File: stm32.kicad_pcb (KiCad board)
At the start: 2 copper layers, 16 parts, among them J1 TC2030, SW1 SW_Push, U1 STM32F411CEUx, Y1 Crystal_GND24

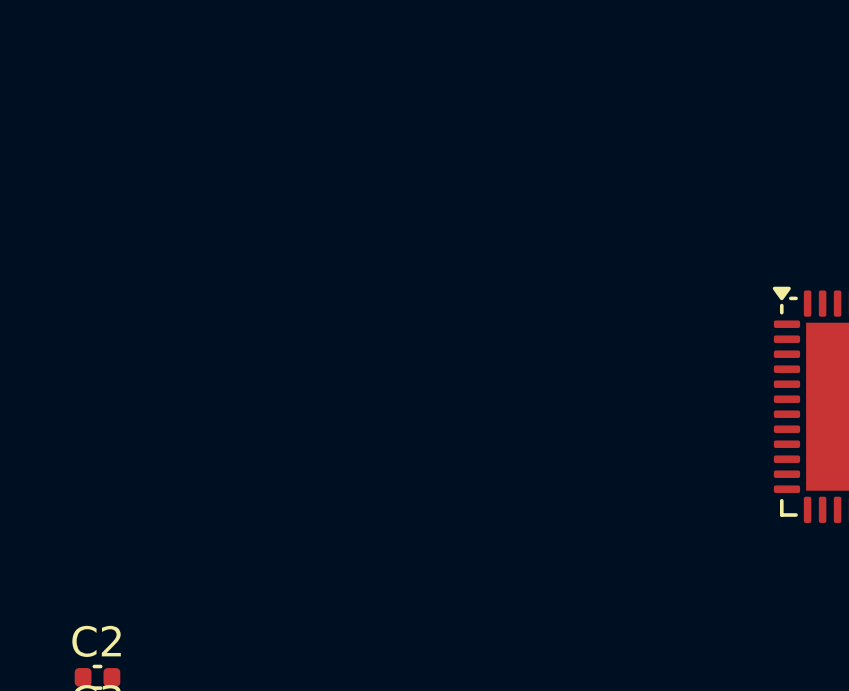
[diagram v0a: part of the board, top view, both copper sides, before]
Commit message: SPI section: place BMI088, BMP388, W25Q128 symbols + decoupling + HOLD/WP pull-ups
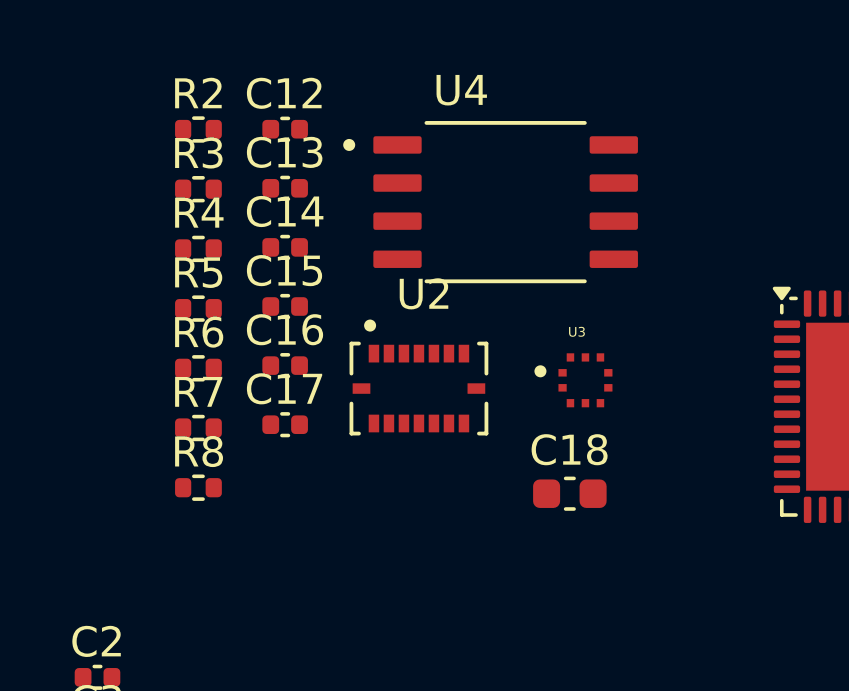
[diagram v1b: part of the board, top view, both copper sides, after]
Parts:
- added C12: 1u, Capacitor_SMD:C_0402_1005Metric, F.Cu at (131.7, 45.9)
- added C13: 100n, Capacitor_SMD:C_0402_1005Metric, F.Cu at (131.7, 47.8)
- added C14: 100n, Capacitor_SMD:C_0402_1005Metric, F.Cu at (131.7, 49.8)
- added C15: 100n, Capacitor_SMD:C_0402_1005Metric, F.Cu at (131.7, 51.8)
- added C16: 100n, Capacitor_SMD:C_0402_1005Metric, F.Cu at (131.7, 53.7)
- added C17: 100n, Capacitor_SMD:C_0402_1005Metric, F.Cu at (131.7, 55.7)
- added C18: 4.7u, Capacitor_SMD:C_0603_1608Metric, F.Cu at (141.2, 58.0)
- added R2: 10k, Resistor_SMD:R_0402_1005Metric, F.Cu at (128.8, 45.9)
- added R3: 10k, Resistor_SMD:R_0402_1005Metric, F.Cu at (128.8, 47.9)
- added R4: 10k, Resistor_SMD:R_0402_1005Metric, F.Cu at (128.8, 49.8)
- added R5: 10k, Resistor_SMD:R_0402_1005Metric, F.Cu at (128.8, 51.8)
- added R6: 10k, Resistor_SMD:R_0402_1005Metric, F.Cu at (128.8, 53.8)
- added R7: 10k, Resistor_SMD:R_0402_1005Metric, F.Cu at (128.8, 55.8)
- added R8: 10k, Resistor_SMD:R_0402_1005Metric, F.Cu at (128.8, 57.8)
- added U2: BMI088, Custom_Library:BMI088, F.Cu at (136.2, 54.5)
- added U3: BMP388, Custom_Library:BMP388, F.Cu at (141.7, 54.2)
- added U4: W25Q128JVSIQ, Custom_Library:W25Q128, F.Cu at (139.1, 48.3)
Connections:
- U1 pad 11: unconnected-(U1-PA1-Pad11) -> /FLASH
- U1 pad 12: unconnected-(U1-PA2-Pad12) -> /BMP
- U1 pad 13: unconnected-(U1-PA3-Pad13) -> /GYRO
- U1 pad 14: unconnected-(U1-PA4-Pad14) -> /ACCEL
- U1 pad 15: unconnected-(U1-PA5-Pad15) -> /SPI1_SCK
- U1 pad 16: unconnected-(U1-PA6-Pad16) -> /SPI1_MISO
- U1 pad 17: unconnected-(U1-PA7-Pad17) -> /SPI1_MOSI
- U1 pad 18: unconnected-(U1-PB0-Pad18) -> /ACCEL_INT
- U1 pad 19: unconnected-(U1-PB1-Pad19) -> /GYRO_INT

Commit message: small update
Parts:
- added J2: USB_C_Receptacle_PowerOnly_6P, Connector_USB:USB_C_Receptacle_GCT_USB4125-xx-x_6P_TopMnt_Horizontal, F.Cu at (121.0, 35.0)
- added R10: 10k, Resistor_SMD:R_0402_1005Metric, F.Cu at (107.8, 34.4)
- added R11: 1k, Resistor_SMD:R_0402_1005Metric, F.Cu at (107.8, 36.4)
- added R12: 1k, Resistor_SMD:R_0402_1005Metric, F.Cu at (107.8, 38.4)
- added R23: 5.1k, Resistor_SMD:R_0402_1005Metric, F.Cu at (107.8, 40.4)
- added R24: 5.1k, Resistor_SMD:R_0402_1005Metric, F.Cu at (107.8, 42.4)
- added R9: 4.7k, Resistor_SMD:R_0402_1005Metric, F.Cu at (107.8, 32.4)
- added U5: TP4056-42-ESOP8, Package_SO:SOIC-8-1EP_3.9x4.9mm_P1.27mm_EP2.41x3.3mm_ThermalVias, F.Cu at (117.8, 48.7)
- added U6: AP63203WU, Package_TO_SOT_SMD:TSOT-23-6, F.Cu at (105.4, 47.8)

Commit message: fleshed out buck
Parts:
- added C19: 1u, Capacitor_SMD:C_0402_1005Metric, F.Cu at (120.6, 94.3)
- added C20: 10u, Capacitor_SMD:C_0603_1608Metric, F.Cu at (129.0, 83.6)
- added C21: 22u, Capacitor_SMD:C_0603_1608Metric, F.Cu at (129.0, 86.1)
- added D1: RED_LED, LED_SMD:LED_Kingbright_KPBD-3224, F.Cu at (121.1, 85.5)
- added D2: GREEN_LED, LED_SMD:LED_Kingbright_KPBD-3224, F.Cu at (125.1, 85.5)
- added IC1: LTC3621EMS8E-3.3#PBF, Custom_Library:LTC3621EMS8E-3.3#PBF, F.Cu at (122.8, 91.0)
- added L1: 4.7u, Inductor_SMD:L_Coilcraft_XxL4020, F.Cu at (129.3, 91.5)

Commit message: next steps
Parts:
- added D3: SS14, Diode_SMD:D_SMA, F.Cu at (147.5, 92.5)
- added D4: 1N4148WS, Diode_SMD:D_SOD-323, F.Cu at (147.5, 88.5)
- added Q1: DMG2305UX, Custom_Library:DMG2305UX, F.Cu at (142.0, 89.5)
- added R13: 100k, Resistor_SMD:R_0402_1005Metric, F.Cu at (147.0, 84.0)
- Y1: value Crystal_GND24 -> 25MHz
- moved J2 76.5 mm to (137.7, 109.7)
- moved SW1 31.6 mm to (120.5, 73.0), turned to 180 degrees
- moved C8 27.5 mm to (138.2, 85.0)
- moved U1 24.2 mm to (136.8, 73.9)
- moved C2 20.4 mm to (139.5, 79.0), turned to -90 degrees
- moved C20 17.3 mm to (142.0, 95.0), turned to -90 degrees
- moved C3 17.2 mm to (142.0, 71.0)
- moved IC1 15.4 mm to (137.8, 94.5), turned to 180 degrees
- moved C10 14.9 mm to (149.9, 64.2)
- moved C11 14.9 mm to (149.9, 66.2)
- moved Y1 14.9 mm to (154.0, 63.5)
- moved C19 12.5 mm to (133.0, 95.0), turned to 180 degrees
- moved L1 12.2 mm to (139.0, 99.0)
- moved C6 10.8 mm to (128.0, 75.5), turned to -90 degrees
- moved J1 8.68 mm to (155.3, 92.1)
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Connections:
- net +5V renamed /VBUS_5V
- C19 pad 1: GND -> Net-(IC1-INTVCC)
- C19 pad 2: Net-(IC1-INTVCC) -> GND
- IC1 pad 7: unconnected-(IC1-MODE/SYNC-Pad7) -> Net-(IC1-INTVCC)
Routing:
- net +3.3V: track 0.00 -> 39.6 mm
- net /NRST: track 0.00 -> 18.3 mm
- net /VIN_BUCK: track 0.00 -> 10.5 mm
- net GND: track 0.00 -> 8.89 mm
- net /GATE_LS: track 0.00 -> 8.05 mm
- net Net-(IC1-SW): track 0.00 -> 3.58 mm
- net Net-(IC1-INTVCC): track 0.00 -> 2.91 mm

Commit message: Assign J5 UART header footprint; import netlist to PCB for layout
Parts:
- added C22: 0.1u, Capacitor_SMD:C_0402_1005Metric, F.Cu at (133.5, 23.9)
- added C23: 100n, Capacitor_SMD:C_0402_1005Metric, F.Cu at (133.5, 25.9)
- added C24: 100n, Capacitor_SMD:C_0402_1005Metric, F.Cu at (133.5, 27.8)
- added D5: LED, LED_SMD:LED_0603_1608Metric, F.Cu at (123.9, 40.6)
- added J3: Conn_01x02, Connector_JST:JST_PH_S2B-PH-SM4-TB_1x02-1MP_P2.00mm_Horizontal, F.Cu at (127.0, 28.5)
- added J4: Conn_01x02, Connector_PinHeader_2.54mm:PinHeader_1x02_P2.54mm_Vertical, F.Cu at (135.0, 36.5)
- added J5: Conn_01x03, Connector_PinHeader_2.54mm:PinHeader_1x03_P2.54mm_Vertical, F.Cu at (114.5, 31.7)
- added R14: 100, Resistor_SMD:R_0402_1005Metric, F.Cu at (120.4, 23.9)
- added R15: 1k, Resistor_SMD:R_0402_1005Metric, F.Cu at (120.4, 25.9)
- added R16: 1k, Resistor_SMD:R_0402_1005Metric, F.Cu at (120.4, 27.9)
- added R17: 10k, Resistor_SMD:R_0402_1005Metric, F.Cu at (120.4, 29.9)
- added R18: 100k, Resistor_SMD:R_0402_1005Metric, F.Cu at (120.4, 31.9)
- added R19: 100k, Resistor_SMD:R_0402_1005Metric, F.Cu at (120.4, 33.9)
- added R20: 0R, Resistor_SMD:R_0402_1005Metric, F.Cu at (120.4, 35.9)
- added R21: 0R, Resistor_SMD:R_0402_1005Metric, F.Cu at (120.4, 37.8)
- added SW2: SW_Push, Button_Switch_SMD:SW_SPST_CK_RS282G05A3, F.Cu at (127.3, 36.7)
- added U6: DW01A, Package_TO_SOT_SMD:SOT-23-6, F.Cu at (134.7, 31.2)
- moved U3 24.4 mm to (153.2, 75.8)
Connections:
- C10 pad 2: /PH0-OSC_OUT -> /OSC_OUT
- C11 pad 2: /PH0-OSC_IN -> /OSC_IN
- Q1 pad 2: /BAT_OUT -> /VIN_BUCK
- Q1 pad 3: /VIN_BUCK -> /Bat+
- U1 pad 10: unconnected-(U1-PA0-Pad10) -> /VBAT_SENSE
- U1 pad 15: /SPI1_SCK -> /SCK_MCU
- U1 pad 17: /SPI1_MOSI -> /MOSI_MCU
- U1 pad 30: unconnected-(U1-PA9-Pad30) -> /UART_TX
- U1 pad 31: unconnected-(U1-PA10-Pad31) -> /UART_RX
- U1 pad 40: unconnected-(U1-PB4-Pad40) -> /LOG_BTN
- U1 pad 41: unconnected-(U1-PB5-Pad41) -> /LED_HB
- U1 pad 5: unconnected-(U1-PH0-Pad5) -> /OSC_IN
- U1 pad 6: unconnected-(U1-PH1-Pad6) -> /OSC_OUT
- U5 pad 1: Net-(U5-TEMP) -> GND
- Y1 pad 1: /PH0-OSC_IN -> /OSC_IN
- Y1 pad 3: /PH0-OSC_OUT -> /OSC_OUT
